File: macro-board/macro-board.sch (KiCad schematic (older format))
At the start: 66 parts, among them SW1 SW_Push, U1 ATmega32U2-AU, Y1 16MHz

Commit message: basically finalize pcb
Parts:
- added D17, D18, D19, D20: WS2812B, LED_SMD:LED_WS2812B_PLCC4_5.0x5.0mm_P3.2mm, symbol LED:WS2812B
- added Q1: Q_NPN_BEC, symbol Device:Q_NPN_BEC
- added R23: 10k, symbol Device:R_Small
- gave numbers to parts that had none: 12
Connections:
- net +5V: now also MX10.3 (LED), MX11.3 (LED), MX14.3 (LED), MX15.3 (LED), MX2.3 (LED), MX3.3 (LED), MX6.3 (LED), MX7.3 (LED), D17.1 (VDD), D18.1 (VDD), D19.1 (VDD), D20.1 (VDD)
- net GND: now also D17.3 (VSS), D18.3 (VSS), D19.3 (VSS), D20.3 (VSS), Q1.2 (E)
- net RGBLED: now reaches U1.19 (PB5)
- net RGBLED: now also D17.4 (DIN)
- net at U1.21 (PB7): now also R23.2
- net LEGEND renamed LEDGND
- net LEDGND: now also Q1.3 (C)
- new net: D17.2 (DOUT), D18.4 (DIN)
- new net: D18.2 (DOUT), D19.4 (DIN)
- new net: D19.2 (DOUT), D20.4 (DIN)
- new net: Q1.1 (B), R23.1
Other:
- moved on the sheet: D1, F1, R5, R6, USB1

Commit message: changes before assigning footprint
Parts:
- added C10, C7, C8, C9: 0.1u, symbol Device:C_Small
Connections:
- net +5V: now also C10.1, C7.1, C8.1, C9.1
- net GND: now also C10.2, C7.2, C8.2, C9.2
- net ROW1: now also D5.1 (K), D6.1 (K), D7.1 (K), D8.1 (K)
- net ROW2: now also D10.1 (K), D11.1 (K), D12.1 (K), D9.1 (K)
- net ROW3: now also D13.1 (K), D14.1 (K), D15.1 (K), D16.1 (K)
- no-connect marks 0 -> 3
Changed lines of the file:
@@
 	3100 3650 3250 3650
-$Comp
-L Device:C_Small C4
-U 1 1 5E5BFE41
-P 700 2900
-F 0 "C4" H 792 2946 50  0000 L CNN
-F 1 "0.1u" H 792 2855 50  0000 L CNN
-F 2 "" H 700 2900 50  0001 C CNN
-F 3 "~" H 700 2900 50  0001 C CNN
-	1    700  2900
-	1    0    0    -1
-$EndComp
 $Comp
 L Device:C_Small C5
@@
 Wire Wire Line
 	7800 3650 7850 3650
-Wire Wire Line
-	5800 3900 6200 3900
 Connection ~ 6200 3900
 Wire Wire Line
@@
 Wire Wire Line
 	7200 3900 7700 3900
-Wire Wire Line
-	5800 3250 6200 3250
 Connection ~ 6200 3250
 Wire Wire Line
@@
 Wire Wire Line
 	7200 3250 7700 3250
-Wire Wire Line
-	5800 2600 6200 2600
 Connection ~ 6200 2600
 Wire Wire Line
@@
 Connection ~ 6900 1150
 Connection ~ 6400 1150
+Wire Wire Line
+	5750 2600 6200 2600
+Wire Wire Line
+	5750 3250 6200 3250
+Wire Wire Line
+	5750 3900 6200 3900
+$Comp
+L Device:C_Small C7
+U 1 1 5E5CFCB9
+P 6350 5250
+F 0 "C7" H 6442 5296 50  0000 L CNN
+F 1 "0.1u" H 6442 5205 50  0000 L CNN
+F 2 "" H 6350 5250 50  0001 C CNN
+F 3 "~" H 6350 5250 50  0001 C CNN
+	1    6350 5250
+	1    0    0    -1
+$EndComp
+$Comp
+L Device:C_Small C8
+U 1 1 5E5D0257
+P 6650 5250
+F 0 "C8" H 6742 5296 50  0000 L CNN
+F 1 "0.1u" H 6742 5205 50  0000 L CNN
+F 2 "" H 6650 5250 50  0001 C CNN
+F 3 "~" H 6650 5250 50  0001 C CNN
+	1    6650 5250
+	1    0    0    -1
+$EndComp
+$Comp
+L Device:C_Small C9
+U 1 1 5E5D0C32
+P 6950 5250
+F 0 "C9" H 7042 5296 50  0000 L CNN
+F 1 "0.1u" H 7042 5205 50  0000 L CNN
+F 2 "" H 6950 5250 50  0001 C CNN
+F 3 "~" H 6950 5250 50  0001 C CNN
+	1    6950 5250
+	1    0    0    -1
+$EndComp
+$Comp
+L Device:C_Small C10
+U 1 1 5E5D0F66
+P 7250 5250
+F 0 "C10" H 7342 5296 50  0000 L CNN
+F 1 "0.1u" H 7342 5205 50  0000 L CNN
+F 2 "" H 7250 5250 50  0001 C CNN
+F 3 "~" H 7250 5250 50  0001 C CNN
+	1    7250 5250
+	1    0    0    -1
+$EndComp
+$Comp
+L Device:C_Small C4
+U 1 1 5E5BFE41
+P 700 2900
+F 0 "C4" H 792 2946 50  0000 L CNN
+F 1 "0.1u" H 792 2855 50  0000 L CNN
+F 2 "" H 700 2900 50  0001 C CNN
+F 3 "~" H 700 2900 50  0001 C CNN
+	1    700  2900
+	1    0    0    -1
+$EndComp
+$Comp
+L power:GND #PWR?
+U 1 1 5E5D1FB9
+P 6200 5350
+F 0 "#PWR?" H 6200 5100 50  0001 C CNN
+F 1 "GND" H 6205 5177 50  0000 C CNN
+F 2 "" H 6200 5350 50  0001 C CNN
+F 3 "" H 6200 5350 50  0001 C CNN
+	1    6200 5350
+	0    1    1    0
+$EndComp
+$Comp
+L power:+5V #PWR?
+U 1 1 5E5D24FA
+P 6200 5150
+F 0 "#PWR?" H 6200 5000 50  0001 C CNN
+F 1 "+5V" H 6215 5323 50  0000 C CNN
+F 2 "" H 6200 5150 50  0001 C CNN
+F 3 "" H 6200 5150 50  0001 C CNN
+	1    6200 5150
+	0    -1   -1   0
+$EndComp
+Wire Wire Line
+	6200 5150 6350 5150
+Connection ~ 6350 5150
+Wire Wire Line
+	6350 5150 6650 5150
+Connection ~ 6650 5150
+Wire Wire Line
+	6650 5150 6950 5150
+Connection ~ 6950 5150
+Wire Wire Line
+	6950 5150 7250 5150
+Wire Wire Line
+	7250 5350 6950 5350
+Connection ~ 6350 5350
+Wire Wire Line
+	6350 5350 6200 5350
+Connection ~ 6650 5350
+Wire Wire Line
+	6650 5350 6350 5350
+Connection ~ 6950 5350
+Wire Wire Line
+	6950 5350 6650 5350
+NoConn ~ 1350 6300
+NoConn ~ 1350 5700
+NoConn ~ 4850 6150
 $EndSCHEMATC

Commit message: add footprint mapping
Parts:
- C1, C10, C2, C3, C4, C5, C6, C7, C8, C9: footprint (none) -> Capacitor_SMD:C_0603_1608Metric
- D1, D10, D11, D12, D13, D14, D15, D16, D2, D3, D4, D5, D6, D7, D8, D9: footprint (none) -> Diode_SMD:D_SOD-123
- D21: renamed from D1; footprint Package_TO_SOT_SMD:SOT-143 -> random-keyboard-parts:SOT143B
- F1: footprint (none) -> Fuse:Fuse_1206_3216Metric
- MX1, MX10, MX11, MX12, MX13, MX14, MX15, MX16, MX2, MX3, MX4, MX5, MX6, MX7, MX8, MX9: footprint (none) -> MX_Alps_Hybrid:MX-1U
- Q1: footprint (none) -> Package_TO_SOT_SMD:SOT-23
- R1, R10, R11, R12, R13, R14, R15, R16, R17, R18, R19, R2, R20, R21, R22, R23, R3, R4, R5, R6, R7, R8, R9: footprint (none) -> Resistor_SMD:R_0805_2012Metric
- SW1: footprint (none) -> random-keyboard-parts:SKQG-1155865
- USB1: footprint (none) -> Type-C:HRO-TYPE-C-31-M-12
- Y1: footprint (none) -> Crystal:Crystal_SMD_3225-4Pin_3.2x2.5mm

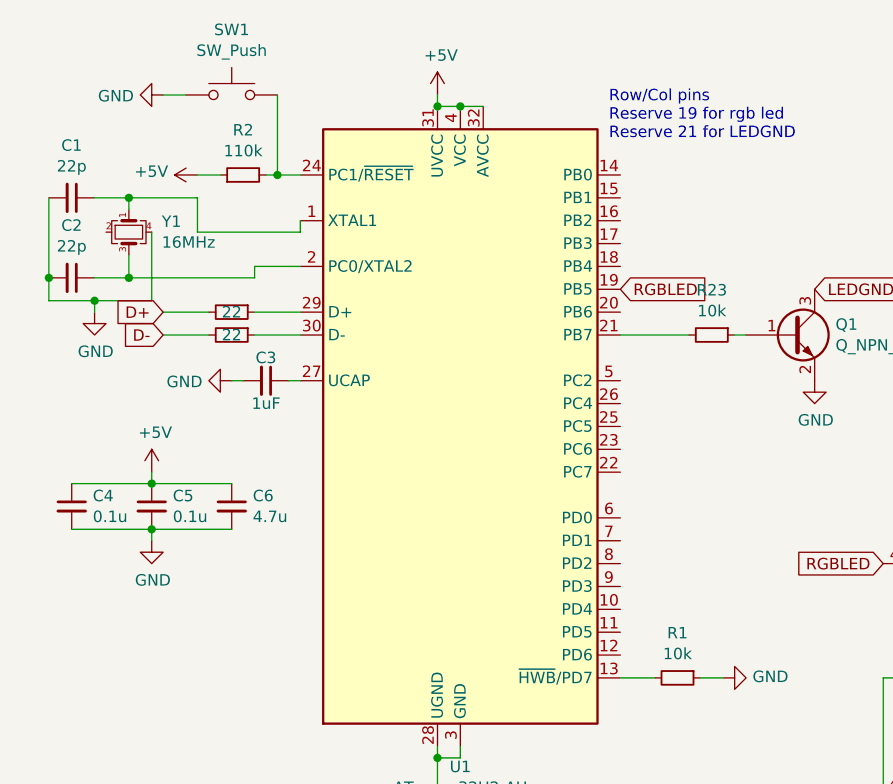
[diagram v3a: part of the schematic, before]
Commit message: finalize routing
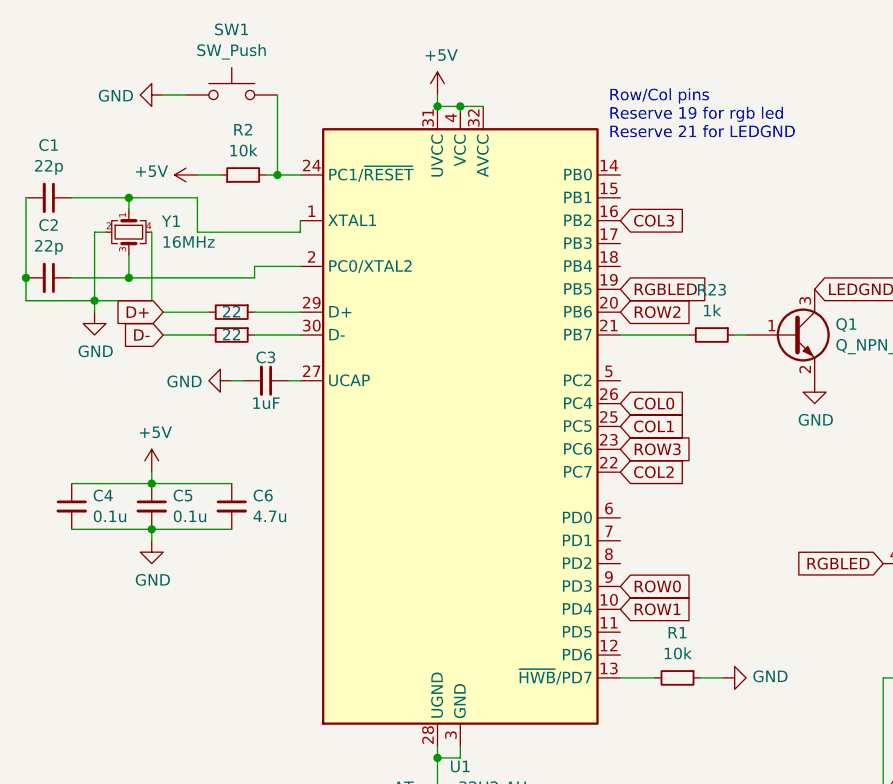
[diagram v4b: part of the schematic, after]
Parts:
- R2: value 110k -> 10k
- R23: value 10k -> 1k
- U1: footprint Package_QFP:TQFP-32_7x7mm_P0.8mm -> Housings_DFN_QFN:QFN-32-1EP_5x5mm_Pitch0.5mm
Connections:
- net COL0: now also U1.26 (PC4)
- net COL1: now also U1.25 (PC5)
- net COL2: now also U1.22 (PC7)
- net COL3: now also U1.16 (PB2)
- net GND: now also Y1.2
- net ROW0: now also U1.9 (PD3)
- net ROW1: now also U1.10 (PD4)
- net ROW2: now also U1.20 (PB6)
- net ROW3: now also U1.23 (PC6)
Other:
- moved on the sheet: C1, C2
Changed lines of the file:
@@
 F 0 "U1" H 2400 1061 50  0000 C CNN
 F 1 "ATmega32U2-AU" H 2400 970 50  0000 C CNN
-F 2 "Package_QFP:TQFP-32_7x7mm_P0.8mm" H 2400 2550 50  0001 C CIN
+F 2 "Housings_DFN_QFN:QFN-32-1EP_5x5mm_Pitch0.5mm" H 2400 2550 50  0001 C CIN
 F 3 "http://ww1.microchip.com/downloads/en/DeviceDoc/doc7799.pdf" H 2400 2550 50  0001 C CNN
 	1    2400 2550
@@
 L Device:C_Small C1
 U 1 1 5E5B6E66
-P 700 1550
-F 0 "C1" V 471 1550 50  0000 C CNN
-F 1 "22p" V 562 1550 50  0000 C CNN
-F 2 "Capacitor_SMD:C_0603_1608Metric" H 700 1550 50  0001 C CNN
-F 3 "~" H 700 1550 50  0001 C CNN
-	1    700  1550
+P 600 1550
+F 0 "C1" V 371 1550 50  0000 C CNN
+F 1 "22p" V 462 1550 50  0000 C CNN
+F 2 "Capacitor_SMD:C_0603_1608Metric" H 600 1550 50  0001 C CNN
+F 3 "~" H 600 1550 50  0001 C CNN
+	1    600  1550
 	0    1    1    0
 $EndComp
@@
 	950  1600 950  1550
 Wire Wire Line
-	950  1550 800  1550
-Wire Wire Line
 	950  1800 950  1900
 Wire Wire Line
-	950  1900 800  1900
-Wire Wire Line
-	600  1900 600  2000
-Wire Wire Line
-	600  2000 800  2000
+	500  1900 500  2000
 Wire Wire Line
 	1050 2000 1050 1700
-Connection ~ 600  1900
+Connection ~ 500  1900
 Wire Wire Line
 	950  1900 1500 1900
@@
 Wire Wire Line
 	800  2050 800  2000
-Connection ~ 800  2000
 Wire Wire Line
 	800  2000 1050 2000
@@
 	1050 2800 1050 2750
 Wire Wire Line
-	600  1900 600  1550
+	500  1900 500  1550
 $Comp
 L Device:C_Small C2
 U 1 1 5E5B7D11
-P 700 1900
-F 0 "C2" V 471 1900 50  0000 C CNN
-F 1 "22p" V 562 1900 50  0000 C CNN
-F 2 "Capacitor_SMD:C_0603_1608Metric" H 700 1900 50  0001 C CNN
-F 3 "~" H 700 1900 50  0001 C CNN
-	1    700  1900
+P 600 1900
+F 0 "C2" V 371 1900 50  0000 C CNN
+F 1 "22p" V 462 1900 50  0000 C CNN
+F 2 "Capacitor_SMD:C_0603_1608Metric" H 600 1900 50  0001 C CNN
+F 3 "~" H 600 1900 50  0001 C CNN
+	1    600  1900
 	0    1    1    0
 $EndComp
@@
 P 1450 1450
 F 0 "R2" V 1646 1450 50  0000 C CNN
-F 1 "110k" V 1555 1450 50  0000 C CNN
+F 1 "10k" V 1555 1450 50  0000 C CNN
 F 2 "Resistor_SMD:R_0805_2012Metric" H 1450 1450 50  0001 C CNN
 F 3 "~" H 1450 1450 50  0001 C CNN
@@
 P 3500 2150
 F 0 "R23" V 3304 2150 50  0000 C CNN
-F 1 "10k" V 3395 2150 50  0000 C CNN
+F 1 "1k" V 3395 2150 50  0000 C CNN
 F 2 "Resistor_SMD:R_0805_2012Metric" H 3500 2150 50  0001 C CNN
 F 3 "~" H 3500 2150 50  0001 C CNN
@@
 	1    0    0    -1
 $EndComp
+Wire Wire Line
+	850  1700 800  1700
+Wire Wire Line
+	700  1900 950  1900
+Wire Wire Line
+	800  1700 800  2000
+Connection ~ 800  2000
+Wire Wire Line
+	500  2000 800  2000
+Wire Wire Line
+	700  1550 950  1550
+Text GLabel 3100 3250 2    50   Input ~ 0
+ROW0
+Text GLabel 3100 3350 2    50   Input ~ 0
+ROW1
+Text GLabel 3100 2050 2    50   Input ~ 0
+ROW2
+Text GLabel 3100 2650 2    50   Input ~ 0
+ROW3
+Text GLabel 3100 1650 2    50   Input ~ 0
+COL3
+Text GLabel 3100 2750 2    50   Input ~ 0
+COL2
+Text GLabel 3100 2550 2    50   Input ~ 0
+COL1
+Text GLabel 3100 2450 2    50   Input ~ 0
+COL0
 $EndSCHEMATC
